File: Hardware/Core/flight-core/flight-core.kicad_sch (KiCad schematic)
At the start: 15 parts, among them J10 Conn_02x05_Counter_Clockwise, J12 Conn_02x05_Counter_Clockwise, J2 Conn_01x08, J20 Conn_01x04, J35 Conn_01x02, J8 Conn_02x05_Counter_Clockwise, J9 Conn_02x05_Counter_Clockwise

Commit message: top sheet reorg
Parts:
- added D17, D18, D19, D20: 60V 3A, obad_footprints:DO-220AA_SS2PH10-M3&slash_84A_VIS, symbol OlinBAD:V3P6L-M3/H
- added J37: Conn_01x02, symbol Connector_Generic:Conn_01x02
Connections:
- net +BATT: now also D17.1 (K), D18.1 (K), D19.1 (K), D20.1 (K)
- net 60V_E: now also D18.2 (A)
- net 60V_N: now also D17.2 (A)
- net 60V_S: now also D19.2 (A)
- net 60V_W: now also D20.2 (A)
- net GND: now also J37.2 (Pin_2)
- net GPIO_SENSE1: now also J2.5 (Pin_5); no longer J2.6 (Pin_6)
- net GPIO_SENSE2: now also J2.6 (Pin_6); no longer J2.7 (Pin_7)
- net GPIO_SENSE3: now also J2.7 (Pin_7); no longer J2.8 (Pin_8)
- new net LVMS: J37.1 (Pin_1)
- new net SENSE_POWER_CYCLE: J2.8 (Pin_8)
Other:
- added sheet Cube 2 Header (cube_1.kicad_sch)
- sheet Power Supplies ports: added LVMS; removed none
- sheet stm32 ports: added SENSE_POWER_CYCLE; removed GPIO_SENSE4
- note added: "BATTERY CONNECTORS"
- note added: "BATTERY LEVEL LOW?"
- note added: "BMS RECEIVE FINAL SHDN?"
- note added: "GPS & SENSE"
- note added: "MASTER SWITCHES"
- note added: "POWER ENABLING CIRCUIT"
- note added: "POWER IN, POWER ENABLE"
- note added: "REMOTE CONTROL?"
- note added: "TILT SENSE?"
- note removed: "HERE BATTERY LEVEL LOW, DIODE 4 IN"
- note removed: "Things left to do: - tilt shutdown? - antenna integration? - i forgot what SENSE_ENABLE was again - power enabling on/off signal"
- note removed: "schottky diode -- 1A, continous power 30W, steady state current is 400mA, 60V, 0.45 voltage drop (schottky), 1/4 watt rated diode (0.45*((3A*5V)/35v)))"
- moved on the sheet: J10, J12, J2, J35, J8, J9, R63, R64, R67, R68, R90, R91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

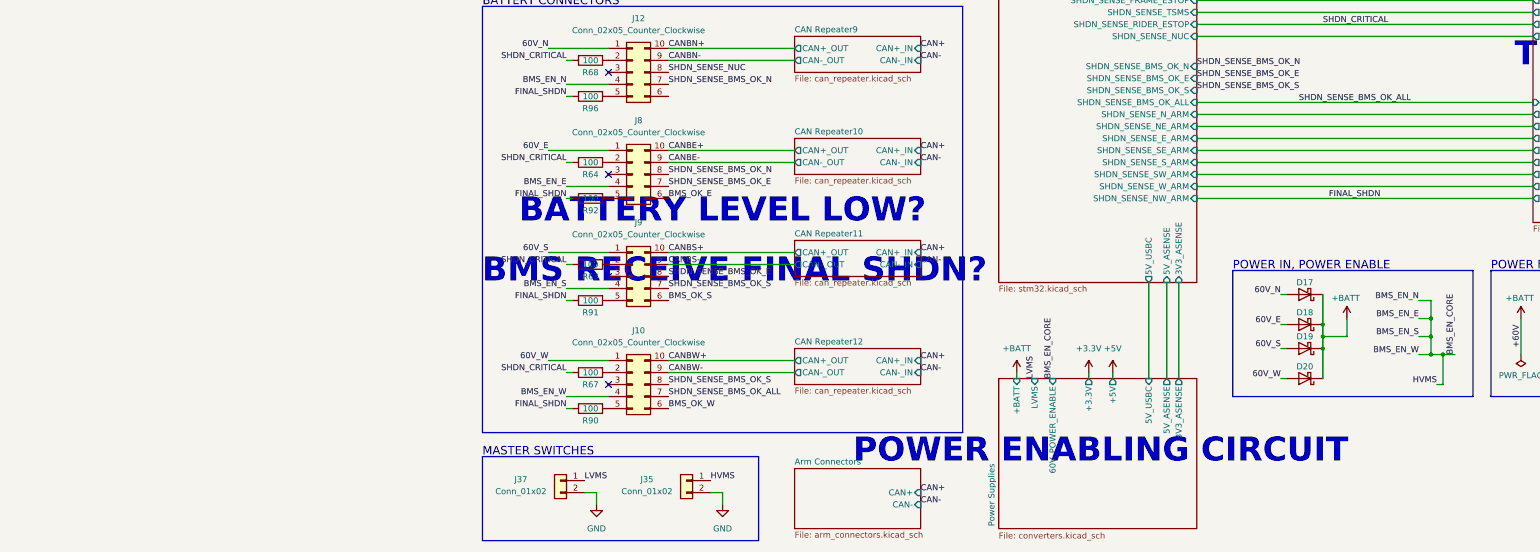
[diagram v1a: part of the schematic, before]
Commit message: updated shutdown and some aux circuits
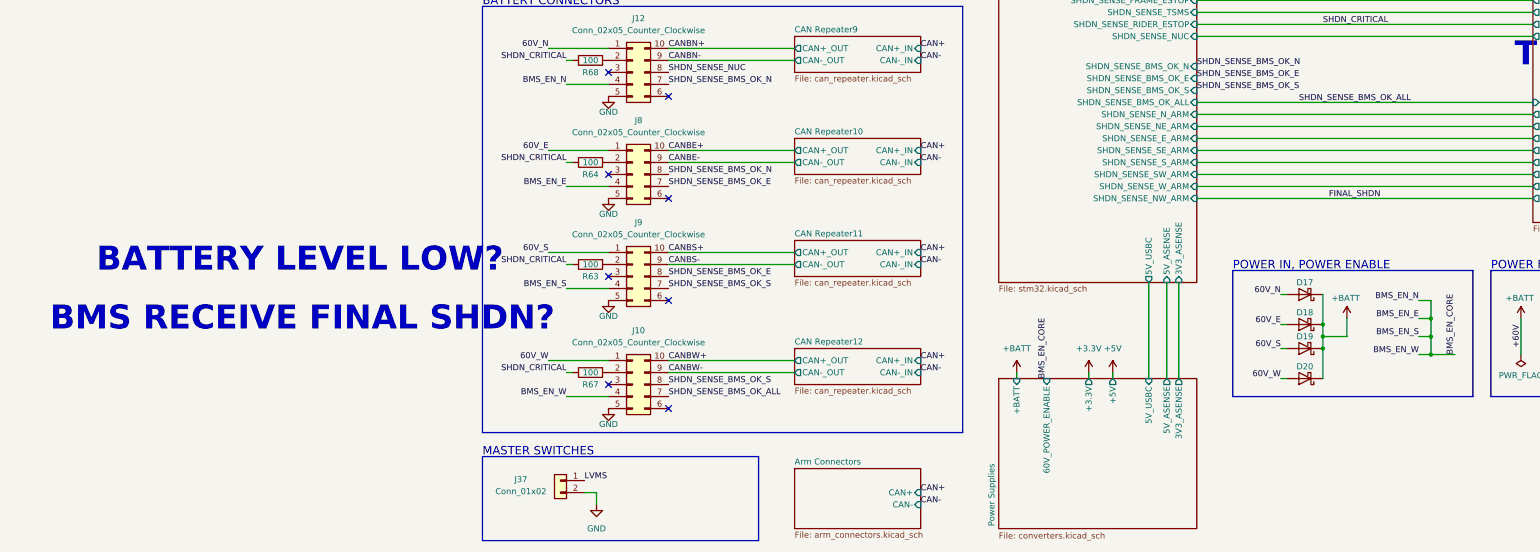
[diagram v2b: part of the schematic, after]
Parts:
- removed J35: Conn_01x02, symbol Connector_Generic:Conn_01x02
- removed R90, R91, R92, R96: 100, footprints:R_0603_1608Metric, symbol Device:R
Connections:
- net GND: now also J10.5 (Pin_5), J12.5 (Pin_5), J8.5 (Pin_5), J9.5 (Pin_5)
- net BMS_OK_E: no longer names the net of J8.6 (Pin_6)
- net BMS_OK_S: no longer names the net of J9.6 (Pin_6)
- net BMS_OK_W: no longer names the net of J10.6 (Pin_6)
- no-connect marks 4 -> 8
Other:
- sheet Power Supplies ports: added none; removed LVMS
- note removed: "POWER ENABLING CIRCUIT"

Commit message: updated all top sheets
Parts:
- removed J2: Conn_01x08, symbol Connector_Generic:Conn_01x08
- removed J20: Conn_01x04, Connector_Molex:Molex_Micro-Fit_3.0_43650-0400_1x04_P3.00mm_Horizontal, symbol Connector_Generic:Conn_01x04
- removed J37: Conn_01x02, symbol Connector_Generic:Conn_01x02
- added J3: Conn_02x02_Remote_ESTOP, Connector_Molex:Molex_Micro-Fit_3.0_43045-0400_2x02_P3.00mm_Horizontal, symbol Connector_Generic:Conn_02x02_Counter_Clockwise
- added J4: Conn_02x04_Counter_Clockwise, symbol Connector_Generic:Conn_02x04_Counter_Clockwise
- added TP16: +3.3V, footprints:Test_Point_SMD, symbol formula:TP_SMD
- added TP25: GND, footprints:Test_Point_SMD, symbol formula:TP_SMD
- added TP30: +60V, footprints:Test_Point_SMD, symbol formula:TP_SMD
- added TP31: +5V, footprints:Test_Point_SMD, symbol formula:TP_SMD
- added TP32: CAN+, footprints:Test_Point_SMD, symbol formula:TP_SMD
- added TP33: CAN-, footprints:Test_Point_SMD, symbol formula:TP_SMD
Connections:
- net +3.3V: now also TP16.1
- net +5V: now also J3.1 (Pin_1), J4.1 (Pin_1), TP31.1
- net +BATT: now also J4.8 (Pin_8), TP30.1
- net CAN+: now also TP32.1, TP33.1
- net CAN+_SENSE: now also J4.6 (Pin_6)
- net CAN-_SENSE: now also J4.5 (Pin_5)
- net CAN_GPS+: now also J3.4 (Pin_4)
- net CAN_GPS-: now also J3.3 (Pin_3)
- net GND: now also J3.2 (Pin_2), J4.7 (Pin_7), TP25.1
- net GPIO_SENSE1: now also J4.3 (Pin_3)
- net GPIO_SENSE2: now also J4.4 (Pin_4)
- net SENSE_POWER_CYCLE: now also J4.2 (Pin_2)
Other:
- removed sheet Arm Connectors
- sheet Cube 1 Header ports: added FINAL_SHDN, SHDN_CRITICAL; removed none
- sheet Cube 2 Header ports: added FINAL_SHDN, SHDN_CRITICAL; removed none
- sheet Shutdown Nodes ports: added CAN+, CAN-, CTRL_CRIT_CHECK, CTRL_NONCRIT_CHECK, LVMS, SHDN_SENSE_CTRL_CRIT, SHDN_SENSE_CTRL_LOBATT; removed CTRL_SANITY_CHECK, SHDN_SENSE_SANITY
- sheet stm32 ports: added CTRL_CRIT_CHECK, CTRL_NONCRIT_CHECK, SHDN_SENSE_CTRL_CRIT, SHDN_SENSE_CTRL_LOBATT; removed CTRL_SANITY_CHECK, GPIO_SENSE3, SHDN_SENSE_SANITY
- note added: "TEST & DEBUG HOOKS"
- note removed: "BATTERY LEVEL LOW?"
- note removed: "BMS RECEIVE FINAL SHDN?"
- note removed: "MASTER SWITCHES"
- note removed: "REMOTE CONTROL?"
- note removed: "TILT SENSE?"

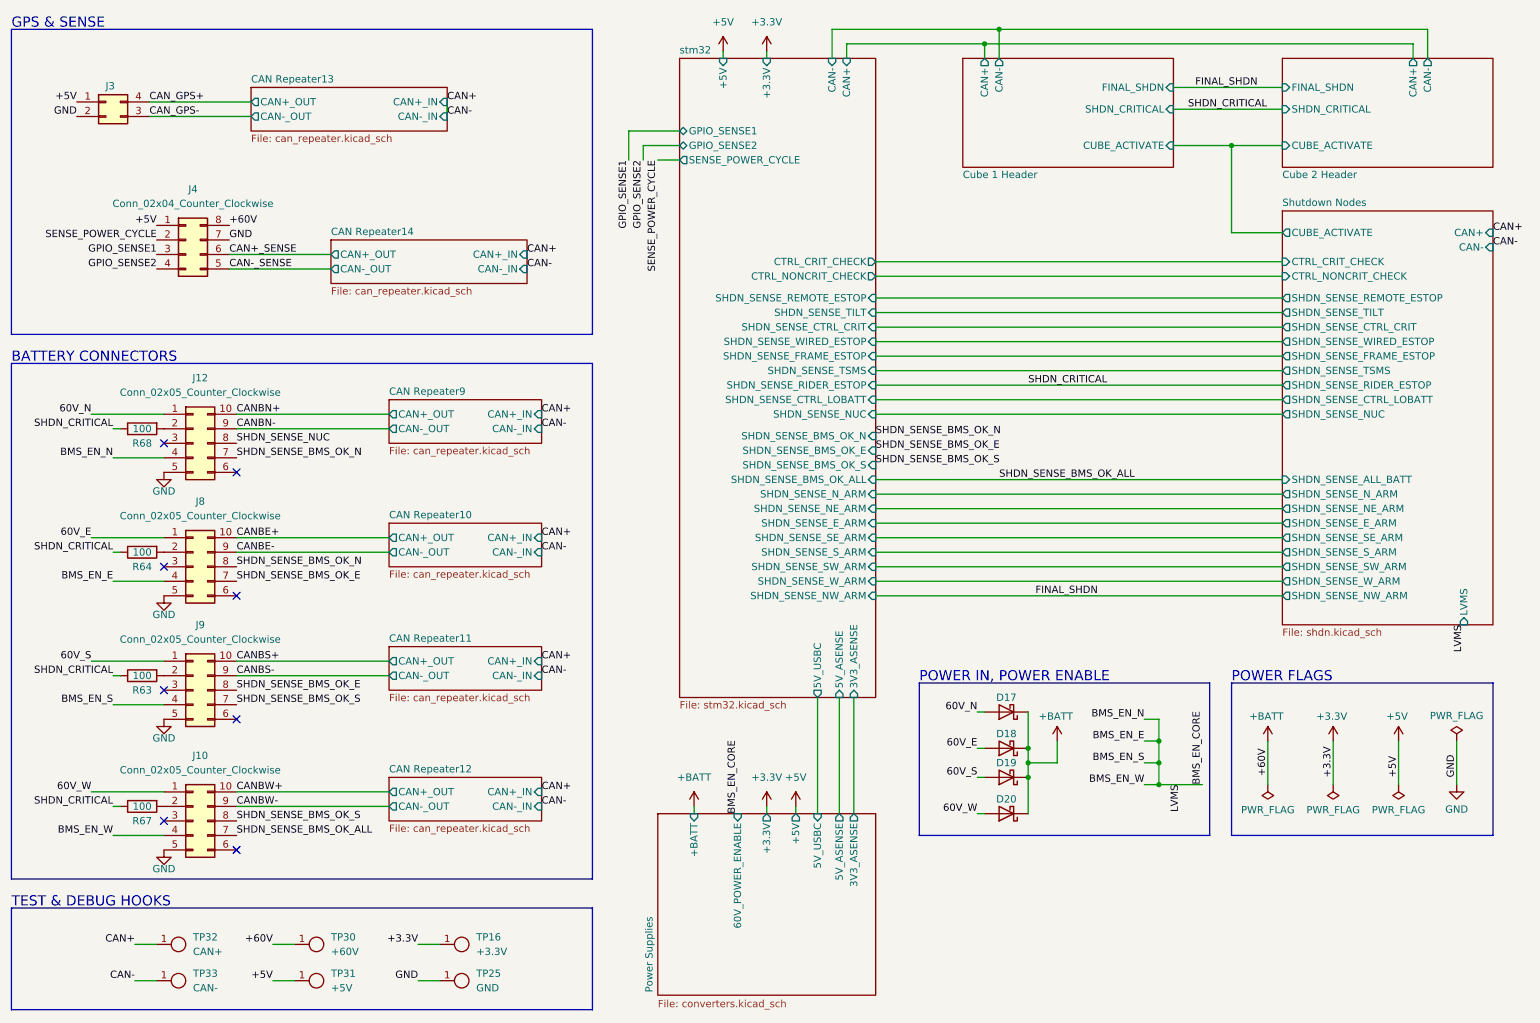
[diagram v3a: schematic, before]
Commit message: corrected CAN+ CAN- accidental connection, added reset_cube
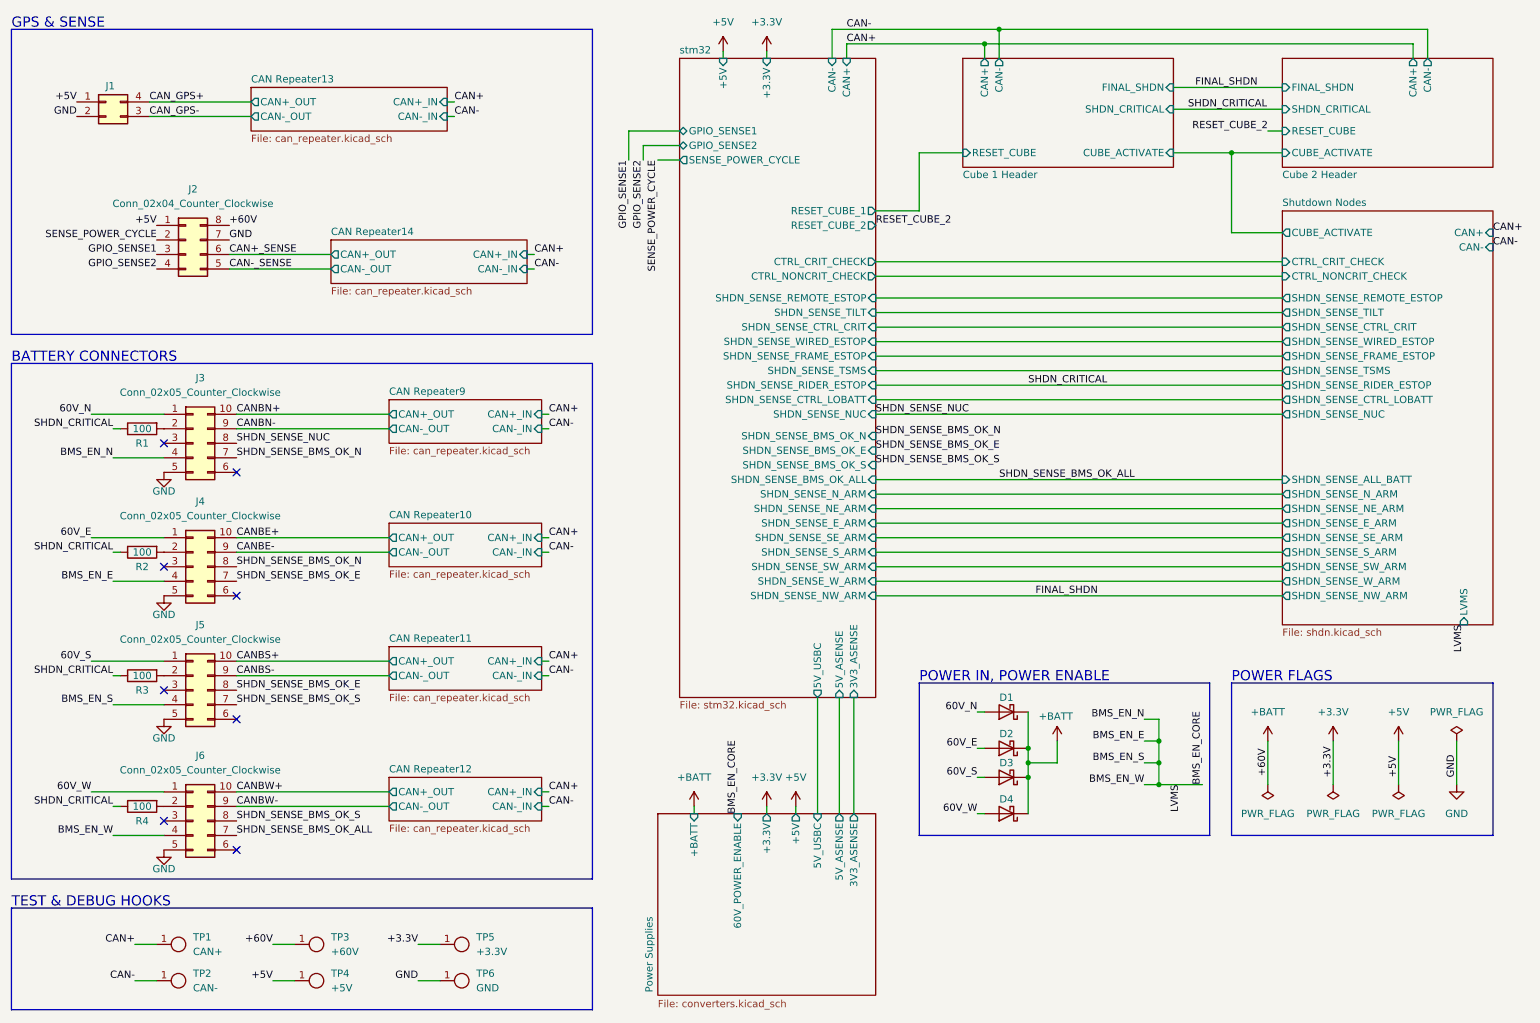
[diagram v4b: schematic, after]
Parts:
- J2: renamed from J4; footprint (none) -> obad_footprints:MicroFit_VT_8
- renumbered D17 to D1, D18 to D2, D19 to D3, D20 to D4, J3 to J1, J12 to J3, J8 to J4, J9 to J5, J10 to J6, R68 to R1, R64 to R2, R63 to R3, R67 to R4, TP32 to TP1, TP33 to TP2, TP30 to TP3, TP31 to TP4, TP16 to TP5, TP25 to TP6
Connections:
- net CAN+: no longer TP2.1
- new net CAN-: TP2.1
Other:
- sheet Cube 1 Header ports: added RESET_CUBE; removed none
- sheet Cube 2 Header ports: added RESET_CUBE; removed none
- sheet stm32 ports: added RESET_CUBE_1, RESET_CUBE_2; removed none

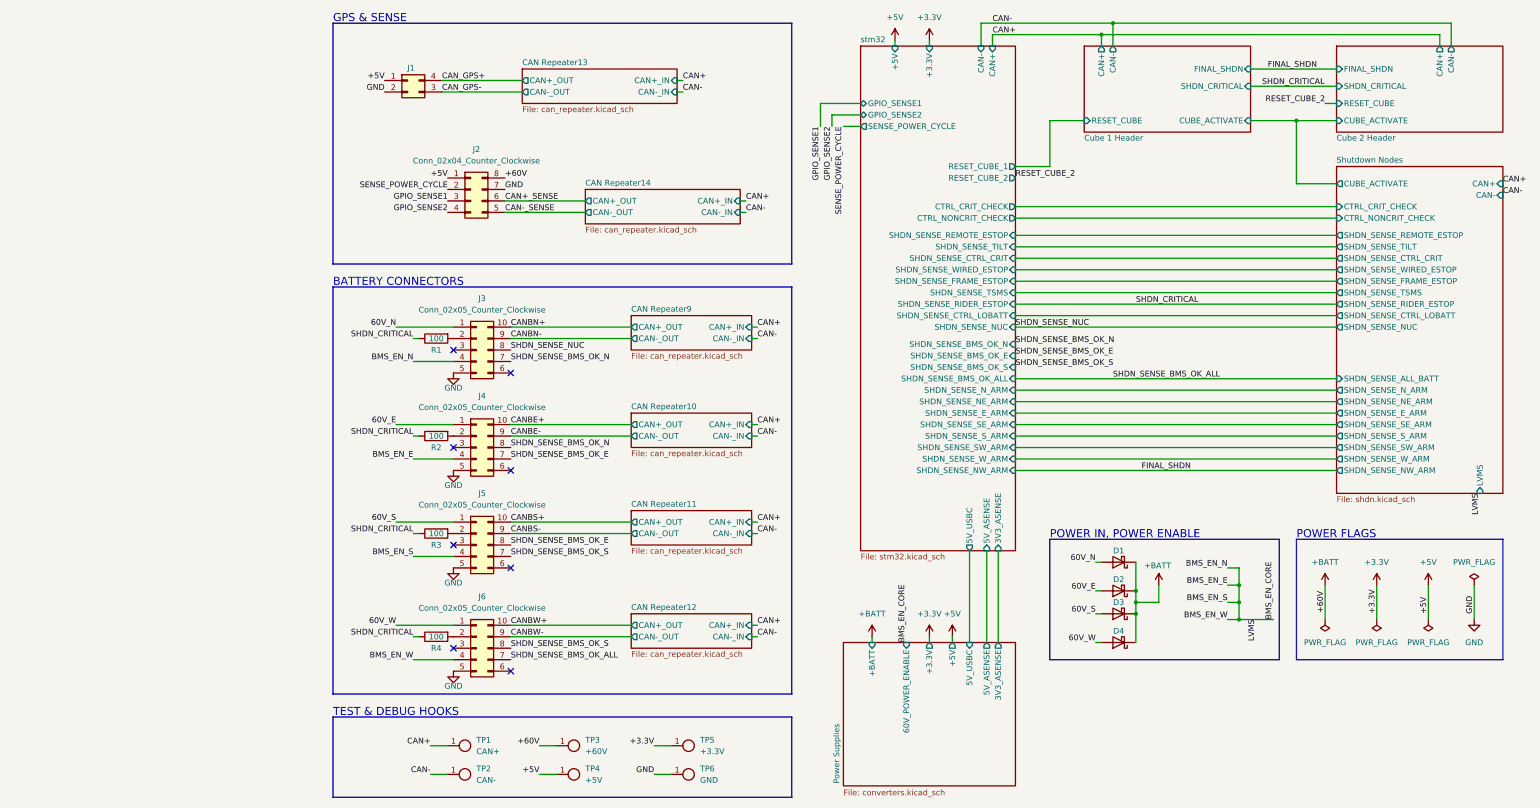
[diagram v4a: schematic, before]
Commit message: major component area placement begun, installing place footprints plugin, updating connectors to vertical
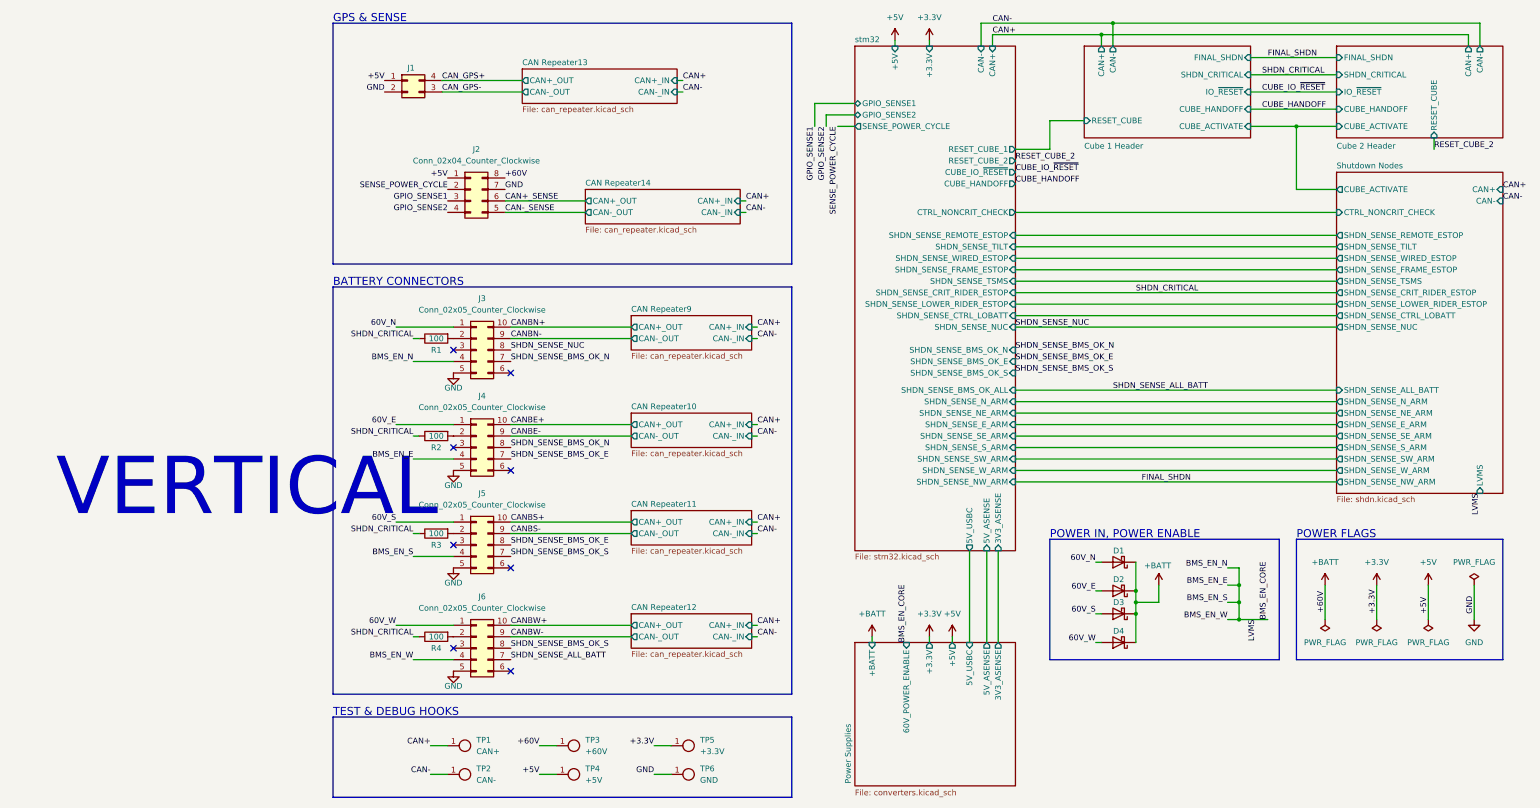
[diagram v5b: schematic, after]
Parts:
- J3, J4, J5, J6: footprint Connector_Molex:Molex_Micro-Fit_3.0_43045-1000_2x05_P3.00mm_Horizontal -> Connector_Molex:Molex_Micro-Fit_3.0_43045-1012_2x05_P3.00mm_Vertical
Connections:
- net SHDN_SENSE_BMS_OK_ALL renamed SHDN_SENSE_ALL_BATT
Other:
- sheet Cube 1 Header ports: added CUBE_HANDOFF, IO_~{RESET}; removed none
- sheet Cube 2 Header ports: added CUBE_HANDOFF, IO_~{RESET}; removed none
- sheet Shutdown Nodes ports: added SHDN_SENSE_CRIT_RIDER_ESTOP, SHDN_SENSE_LOWER_RIDER_ESTOP; removed CTRL_CRIT_CHECK, SHDN_SENSE_CTRL_CRIT, SHDN_SENSE_RIDER_ESTOP
- sheet stm32 ports: added CUBE_HANDOFF, CUBE_IO_~{RESET}, SHDN_SENSE_CRIT_RIDER_ESTOP, SHDN_SENSE_LOWER_RIDER_ESTOP; removed CTRL_CRIT_CHECK, SHDN_SENSE_CTRL_CRIT, SHDN_SENSE_RIDER_ESTOP
- note added: "VERTICAL"

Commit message: can repeater placement, custom cube footprint, connector placement
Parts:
- J1: footprint Connector_Molex:Molex_Micro-Fit_3.0_43045-0400_2x02_P3.00mm_Horizontal -> Connector_Molex:Molex_Micro-Fit_3.0_43045-0412_2x02_P3.00mm_Vertical
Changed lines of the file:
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@@
 			)
 		)
-		(property "Footprint" "Connector_Molex:Molex_Micro-Fit_3.0_43045-0400_2x02_P3.00mm_Horizontal"
+		(property "Footprint" "Connector_Molex:Molex_Micro-Fit_3.0_43045-0412_2x02_P3.00mm_Vertical"
 			(at 35.56 33.02 0)
 			(effects

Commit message: updating mini tps to new symbol and footprint
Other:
- note removed: "VERTICAL"
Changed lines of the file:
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@@
-		)
-	)
-	(text "VERTICAL"
-		(exclude_from_sim no)
-		(at 0 123.19 0)
-		(effects
-			(font
-				(size 12.7 12.7)
-			)
 		)
 	)
@@
 	(wire
 		(pts
+			(xy 170.18 87.63) (xy 241.3 87.63)
+		)
+		(stroke
+			(width 0)
+			(type default)
+		)
+	)
+	(wire
+		(pts
 			(xy 177.8 48.26) (xy 177.8 41.91)
 		)
@@
 		(pts
 			(xy 232.41 43.18) (xy 241.3 43.18)
-		)
-		(stroke
-			(width 0)
-			(type default)
-		)
-	)
-	(wire
-		(pts
-			(xy 170.18 87.63) (xy 241.3 87.63)
 		)
 		(stroke
@@
 	)
 	(label "SHDN_SENSE_NUC"
-		(at 170.18 87.63 0)
-		(effects
-			(font
+		(at 195.58 87.63 0)
+		(effects
+			(font
